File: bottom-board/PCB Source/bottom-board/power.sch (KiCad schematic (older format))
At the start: 30 parts, among them P3 BARREL_JACK, U1 TS2596, U2 LD1117S50TR_SOT223

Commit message: rev 0.0.3
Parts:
- removed C1, C13, C4: 100nF, Capacitor_SMD:C_0603_1608Metric, symbol bottom-board-rescue:C_Small
- removed C11: 10uF, Capacitor_SMD:C_0805_2012Metric, symbol bottom-board-rescue:C_Small-Device
- removed C53, C6, C74: 1000uF, Capacitor_THT:CP_Radial_D10.0mm_P5.00mm, symbol bottom-board-rescue:CP_Small
- removed D3, D4: 1N4148, Diode_SMD:D_SOD-323, symbol Diode:1N4148
- removed H1: MountingHole_Pad, MountingHole:MountingHole_3.2mm_M3_DIN965_Pad, symbol Mechanical:MountingHole_Pad
- removed L3: 1mH, Inductor_SMD:L_Bourns_SRR1260, symbol bottom-board-rescue:FILTER
- removed R8: 10R, Resistor_SMD:R_1206_3216Metric, symbol Device:R_Small
- added C1: 10uF, Capacitor_SMD:CP_Elec_4x5.7, symbol bottom-board-rescue:CP_Small
- added C87: 100nF, Capacitor_SMD:C_0603_1608Metric, symbol bottom-board-rescue:C_Small
- added JP1: Jumper, Jumper:SolderJumper-2_P1.3mm_Bridged2Bar_RoundedPad1.0x1.5mm, symbol bottom-board-rescue:Jumper-Device
- added U9: LD1117S50TR_SOT223, Package_TO_SOT_SMD:SOT-223-3_TabPin2, symbol bottom-board-rescue:LD1117S50TR_SOT223-Regulator_Linear
- C10, C12, C5, C7, C9: MPN C1608X7R1E104K080AA -> GCM188R71C104KA37D
- C2: value 1000uF -> 10uF; footprint Capacitor_THT:CP_Radial_D10.0mm_P5.00mm -> Capacitor_SMD:CP_Elec_4x5.7; MPN 108CKS016M -> EEE-HB1C100R
- D7: symbol Device:D_Shockley -> bottom-board-rescue:D_Shockley-Device
- H5: symbol Mechanical:MountingHole_Pad -> bottom-board-rescue:MountingHole_Pad-Mechanical
- L2: symbol pspice:INDUCTOR -> bottom-board-rescue:INDUCTOR-pspice
- U1: symbol Regulator_Switching:LM2596S-5 -> bottom-board-rescue:LM2596S-5-Regulator_Switching
- U2: value LD1117S50TR_SOT223 -> TL750M10CKVURG3; footprint Package_TO_SOT_SMD:SOT-223-3_TabPin2 -> Package_TO_SOT_SMD:TO-252-3_TabPin2; MPN NCP1117DT50G -> TL750M10CKVURG3
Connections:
- net labels added: +10V
- net labels removed: +12VA
- wire segments 99 -> 71
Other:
- note added: "Only to be merged at codec ground"
- note removed: "CODEC"
- note removed: "Op Amps"
- note removed: "separate ground for analog and digital circuits, passed through the enclosure and lifted"
- moved on the sheet: C10, C8, C9

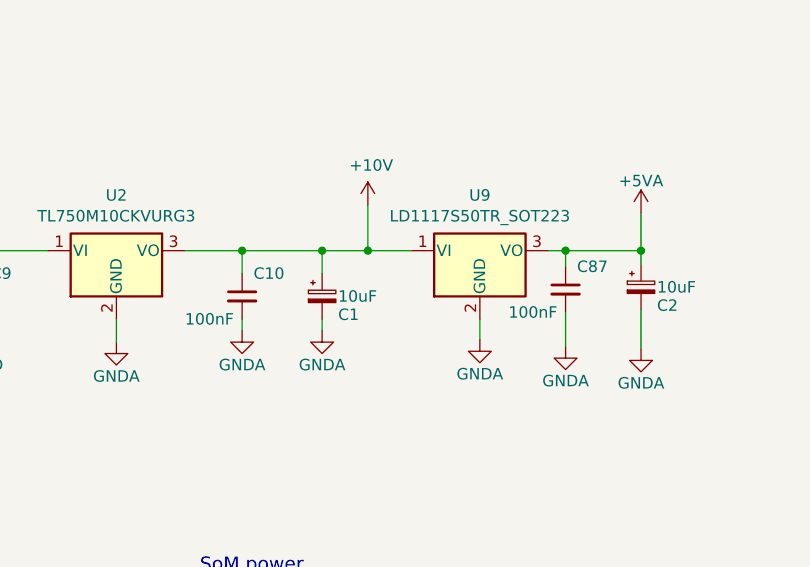
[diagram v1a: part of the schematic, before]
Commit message: change design to 4 layer PCB
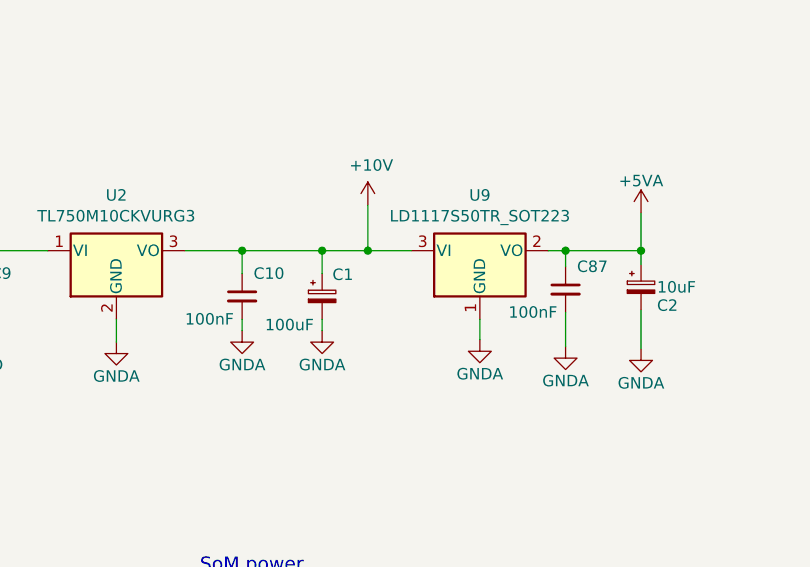
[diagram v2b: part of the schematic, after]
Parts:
- removed U9: LD1117S50TR_SOT223, Package_TO_SOT_SMD:SOT-223-3_TabPin2, symbol bottom-board-rescue:LD1117S50TR_SOT223-Regulator_Linear
- added U9: LD1117S50TR_SOT223, Package_TO_SOT_SMD:SOT-223-3_TabPin2, symbol Regulator_Linear:LD1117S50TR_SOT223
- C1: value 10uF -> 100uF; footprint Capacitor_SMD:CP_Elec_4x5.7 -> Capacitor_SMD:CP_Elec_6.3x7.7; MPN EEE-HB1C100R -> UWX1C101MCL1GB
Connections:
- net +10V: now also U9.3 (VI)
- net +5VA: now also U9.2 (VO)
- net GNDA: now also U9.1 (GND)
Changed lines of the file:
@@
-	1    0    0    -1
-$EndComp
-$Comp
-L bottom-board-rescue:CP_Small C1
-U 1 1 5FD1DD0A
-P 5740 3825
-AR Path="/54F7244B/5FD1DD0A" Ref="C1"  Part="1"
-AR Path="/54F72B97/5FD1DD0A" Ref="C?"  Part="1"
-AR Path="/54F72C8D/5FD1DD0A" Ref="C?"  Part="1"
-F 0 "C1" H 5810 3745 50  0000 L CNN
-F 1 "10uF" H 5810 3825 50  0000 L CNN
-F 2 "Capacitor_SMD:CP_Elec_4x5.7" H 5778 3675 30  0001 C CNN
-F 3 "" H 5740 3825 60  0000 C CNN
-F 4 "EEE-HB1C100R" H 2240 1025 50  0001 C CNN "MPN"
-	1    5740 3825
 	1    0    0    -1
 $EndComp
@@
 Wire Wire Line
 	6115 990  6115 875
-$Comp
-L bottom-board-rescue:LD1117S50TR_SOT223-Regulator_Linear U9
-U 1 1 5F7FE21B
-P 6430 3625
-F 0 "U9" H 6430 3867 50  0000 C CNN
-F 1 "LD1117S50TR_SOT223" H 6430 3776 50  0000 C CNN
-F 2 "Package_TO_SOT_SMD:SOT-223-3_TabPin2" H 6430 3825 50  0001 C CNN
-F 3 "http://www.st.com/st-web-ui/static/active/en/resource/technical/document/datasheet/CD00000544.pdf" H 6530 3375 50  0001 C CNN
-	1    6430 3625
-	1    0    0    -1
-$EndComp
 Wire Wire Line
 	6730 3625 6805 3625
@@
 Wire Wire Line
 	7135 3885 7135 4055
+$Comp
+L bottom-board-rescue:CP_Small C1
+U 1 1 5FB8A0B7
+P 5740 3825
+AR Path="/54F7244B/5FB8A0B7" Ref="C1"  Part="1"
+AR Path="/54F72B97/5FB8A0B7" Ref="C?"  Part="1"
+AR Path="/54F72C8D/5FB8A0B7" Ref="C?"  Part="1"
+AR Path="/54F72CD0/5FB8A0B7" Ref="C?"  Part="1"
+AR Path="/5F5FD115/5FB8A0B7" Ref="C?"  Part="1"
+F 0 "C1" H 5785 3920 50  0000 L CNN
+F 1 "100uF" H 5490 3700 50  0000 L CNN
+F 2 "Capacitor_SMD:CP_Elec_6.3x7.7" H 5778 3675 30  0001 C CNN
+F 3 "" H 5740 3825 60  0000 C CNN
+F 4 "UWX1C101MCL1GB" H 2240 1025 50  0001 C CNN "MPN"
+	1    5740 3825
+	1    0    0    -1
+$EndComp
+$Comp
+L Regulator_Linear:LD1117S50TR_SOT223 U9
+U 1 1 5FD15934
+P 6430 3625
+F 0 "U9" H 6430 3867 50  0000 C CNN
+F 1 "LD1117S50TR_SOT223" H 6430 3776 50  0000 C CNN
+F 2 "Package_TO_SOT_SMD:SOT-223-3_TabPin2" H 6430 3825 50  0001 C CNN
+F 3 "http://www.st.com/st-web-ui/static/active/en/resource/technical/document/datasheet/CD00000544.pdf" H 6530 3375 50  0001 C CNN
+	1    6430 3625
+	1    0    0    -1
+$EndComp
 $EndSCHEMATC
